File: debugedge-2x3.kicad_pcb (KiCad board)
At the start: 2 copper layers, 13 x 15.2 mm, 2 parts, among them J1 Conn_ARM_JTAG_SWD_10, J2 DebugEdge_02x03

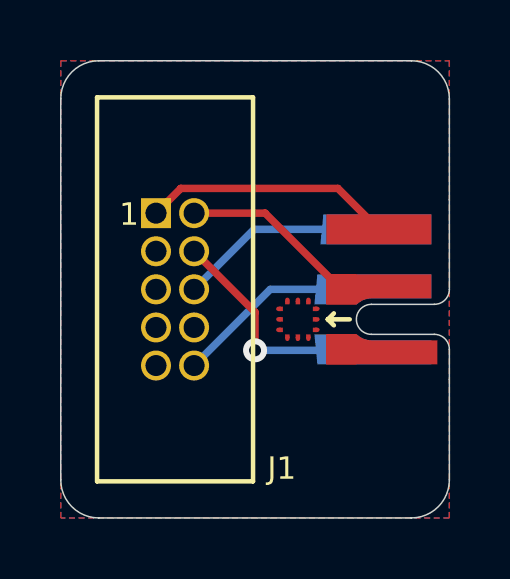
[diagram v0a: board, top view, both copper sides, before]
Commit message: fix wrong connector
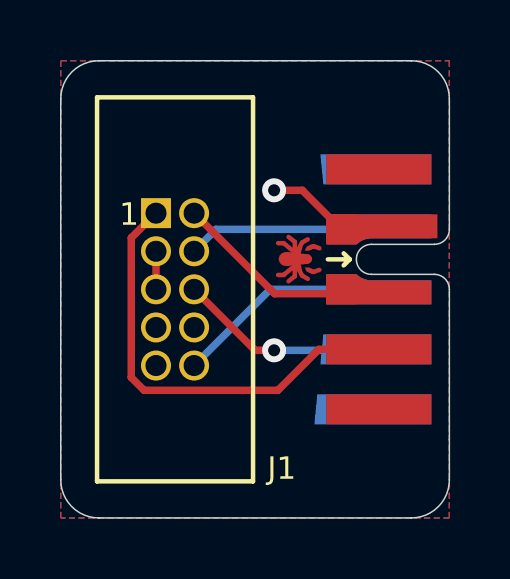
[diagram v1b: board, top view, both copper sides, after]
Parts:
- J2: value DebugEdge_02x03 -> DebugEdge_02x05; footprint Connector_DebugEdge:DebugEdge_2x03_Target -> Connector_DebugEdge:DebugEdge_2x05_Host
- turned J2 to 270 degrees
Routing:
- net +3V3: track 8.34 -> 14.8 mm
- net GND: track 0.00 -> 4.05 mm, vias 0 -> 1
- net /SWDCLK: track 8.53 -> 6.71 mm, vias 1 -> 0
- net /SWO: track 6.94 -> 7.01 mm, vias 0 -> 1
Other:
- outline, holes or cut-outs redrawn
- board text added: "github.com/noahp/ debugedge-2x3 v2"
- board text removed: "github.com/noahp/ debugedge-2x3 v1"
